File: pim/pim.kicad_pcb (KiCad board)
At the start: 2 copper layers, 76.2 x 33 mm, 3 parts, among them J1 Upper pins, J2 Lower pins

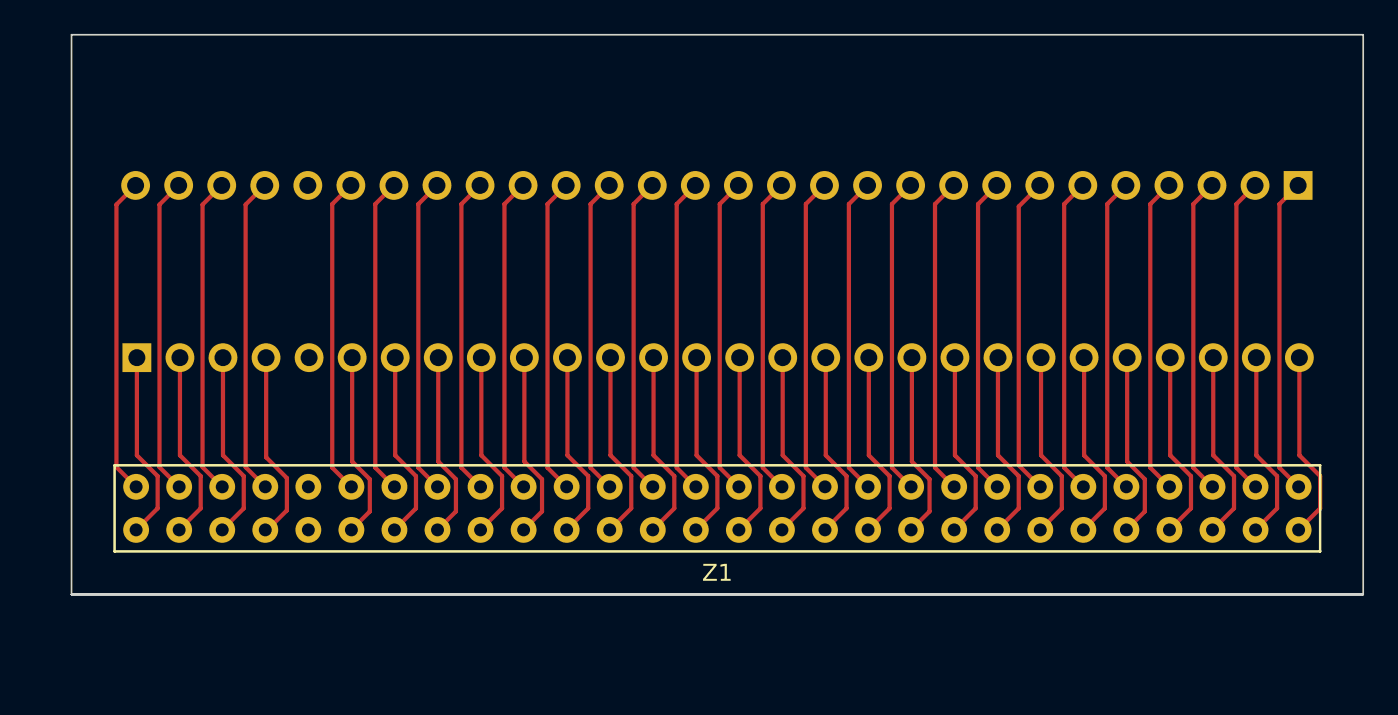
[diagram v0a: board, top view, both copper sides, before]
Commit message: widen connector to match the ones i have
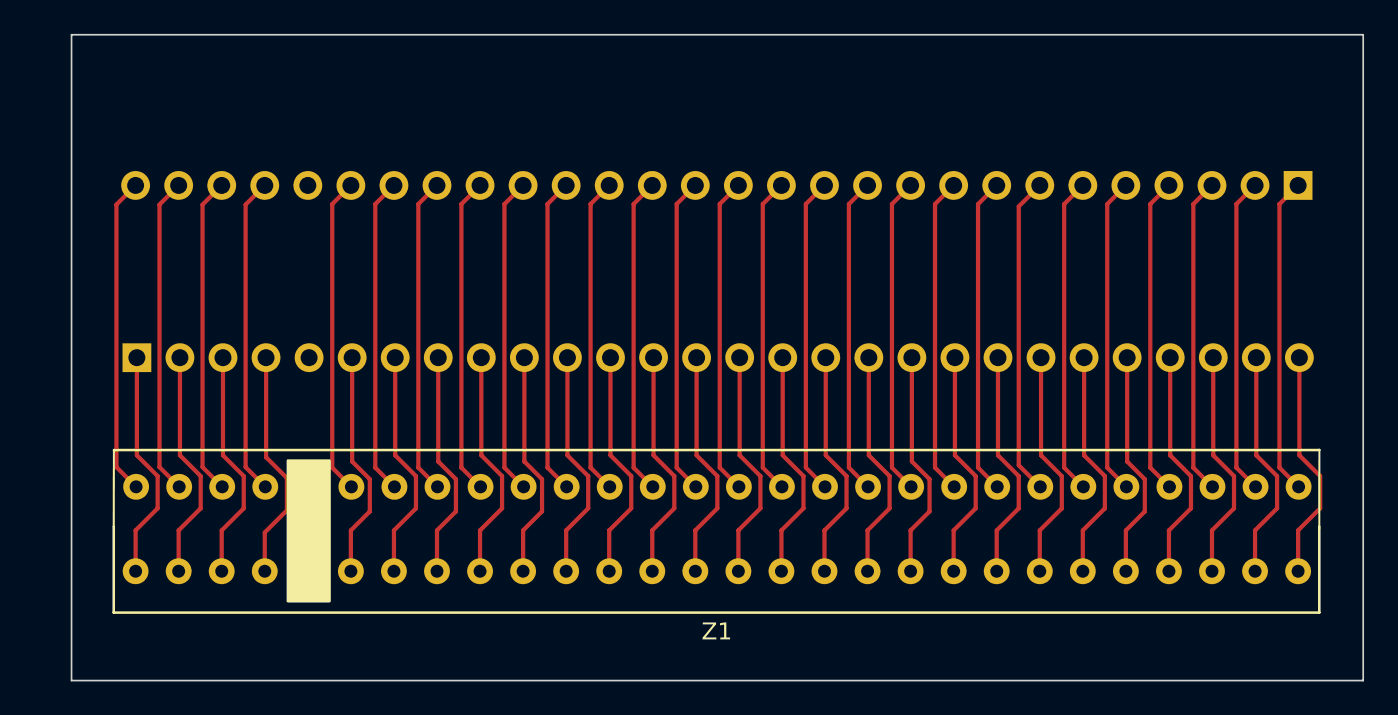
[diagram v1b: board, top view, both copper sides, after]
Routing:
- net V: track 11.2 -> 13.6 mm
- net U: track 11.2 -> 13.6 mm
- net ROMCS: track 11.2 -> 13.6 mm
- net IORQGE: track 11.2 -> 13.6 mm
- net GND3: track 11.2 -> 13.6 mm
- net GND2: track 11.2 -> 13.6 mm
- net BUSACK: track 11.2 -> 13.6 mm
- net A7: track 11.2 -> 13.6 mm
- net A6: track 11.2 -> 13.6 mm
- net A3: track 11.2 -> 13.6 mm
- net A2: track 11.2 -> 13.6 mm
- net A14: track 11.2 -> 13.6 mm
- net A11: track 11.2 -> 13.6 mm
- net A0: track 11.2 -> 13.6 mm
- net +5V: track 11.2 -> 13.6 mm
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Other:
- board size 76.2 x 33 mm -> 76.2 x 38.1 mm

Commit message: ready for a v1.0 fab
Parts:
- added ?: , , F.Cu at (174.1, 112.0)
- added ?: , , F.Cu at (133.5, 108.8)
- added ?: , , F.Cu at (131.0, 108.8)
- added ?: , , F.Cu at (141.1, 112.0)
- added ?: , , F.Cu at (171.6, 108.8)
- added ?: , , F.Cu at (161.4, 108.8)
- added ?: , , F.Cu at (146.2, 112.0)
- added ?: , , F.Cu at (125.8, 112.1)
- added ?: , , F.Cu at (120.7, 112.1)
- added ?: , , F.Cu at (115.6, 112.0)
- added ?: , , F.Cu at (128.4, 112.1)
- added ?: , , F.Cu at (151.3, 108.8)
- added ?: , , F.Cu at (118.2, 108.9)
- added ?: , , F.Cu at (163.9, 108.8)
- added ?: , , F.Cu at (156.3, 112.0)
- added ?: , , F.Cu at (181.8, 108.8)
- added ?: , , F.Cu at (128.5, 108.9)
- added ?: , , F.Cu at (179.2, 112.0)
- added ?: , , F.Cu at (169.0, 112.0)
- added ?: , , F.Cu at (138.5, 112.0)
- added ?: , , F.Cu at (163.9, 112.0)
- added ?: , , F.Cu at (113.1, 108.8)
- added ?: , , F.Cu at (120.7, 108.9)
- added ?: , , F.Cu at (156.4, 108.8)
- added ?: , , F.Cu at (136.0, 108.9)
- added ?: , , F.Cu at (130.9, 112.0)
- added ?: , , F.Cu at (176.7, 108.8)
- added ?: , , F.Cu at (158.9, 108.8)
- added ?: , , F.Cu at (174.1, 108.8)
- added ?: , , F.Cu at (136.0, 112.0)
- added ?: , , F.Cu at (125.9, 108.9)
- added ?: , , F.Cu at (148.8, 108.8)
- added ?: , , F.Cu at (179.2, 108.8)
- added ?: , , F.Cu at (169.1, 108.8)
- added ?: , , F.Cu at (181.8, 112.0)
- added ?: , , F.Cu at (153.8, 108.8)
- added ?: , , F.Cu at (148.7, 112.0)
- added ?: , , F.Cu at (118.2, 112.1)
- added ?: , , F.Cu at (115.7, 108.8)
- added ?: , , F.Cu at (166.4, 108.8)
- added ?: , , F.Cu at (166.4, 112.0)
- added ?: , , F.Cu at (151.3, 112.0)
- added ?: , , F.Cu at (161.4, 112.0)
- added ?: , , F.Cu at (153.8, 112.0)
- added ?: , , F.Cu at (143.7, 108.8)
- added ?: , , F.Cu at (146.2, 108.9)
- added ?: , , F.Cu at (133.4, 112.0)
- added ?: , , F.Cu at (138.6, 108.8)
- added ?: , , F.Cu at (158.9, 112.0)
- added ?: , , F.Cu at (113.1, 112.0)
- added ?: , , F.Cu at (143.6, 112.0)
- added ?: , , F.Cu at (141.1, 108.8)
- added ?: , , F.Cu at (171.6, 112.0)
- added ?: , , F.Cu at (176.6, 112.0)
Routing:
- net A3: track 13.6 -> 17.3 mm
- net U: track 13.6 -> 17.3 mm
- net BUSRQ: track 13.5 -> 17.1 mm
- net A11: track 13.6 -> 17.3 mm
- net Y: track 13.6 -> 17.3 mm
- net A9: track 13.6 -> 17.3 mm
- net A0: track 13.6 -> 17.2 mm
- net RESET: track 13.6 -> 17.2 mm
- net ROMCS: track 13.6 -> 17.2 mm
- net V: track 13.6 -> 17.2 mm
- net A7: track 13.6 -> 17.2 mm
- net IORQGE: track 13.6 -> 17.2 mm
- net A4: track 13.5 -> 17.1 mm
- net CLK: track 13.5 -> 17.1 mm
- net A5: track 13.6 -> 17.2 mm
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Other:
- board size 76.2 x 38.1 mm -> 76.2 x 34.5 mm
- board text added: "+12V"
- board text added: "+12VAC"
- board text added: "+5V"
- board text added: "+9V"
- board text added: "-5V"
- board text added: "A0"
- board text added: "A1"
- board text added: "A10"
- board text added: "A11"
- board text added: "A12"
- board text added: "A13"
- board text added: "A14"
- board text added: "A15"
- board text added: "A2"
- board text added: "A3"
- board text added: "A4"
- board text added: "A5"
- board text added: "A6"
- board text added: "A7"
- board text added: "A8"
- board text added: "A9"
- board text added: "BUSACK"
- board text added: "BUSRQ"
- board text added: "CLK"
- board text added: "D0"
- board text added: "D1"
- board text added: "D2"
- board text added: "D3"
- board text added: "D4"
- board text added: "D5"
- board text added: "D6"
- board text added: "D7"
- board text added: "GND"
- board text added: "HALT"
- board text added: "INT"
- board text added: "IORQ"
- board text added: "IORQGE"
- board text added: "M1"
- board text added: "MREQ"
- board text added: "NC"
- board text added: "NMI"
- board text added: "RD"
- board text added: "RESET"
- board text added: "RFSH"
- board text added: "ROMCS"
- board text added: "U"
- board text added: "V"
- board text added: "VIDEO"
- board text added: "WAIT"
- board text added: "WR"
- board text added: "Y"
- board text added: "github.com/derekfountain/zx-spectrum-plugin-module v1.0"

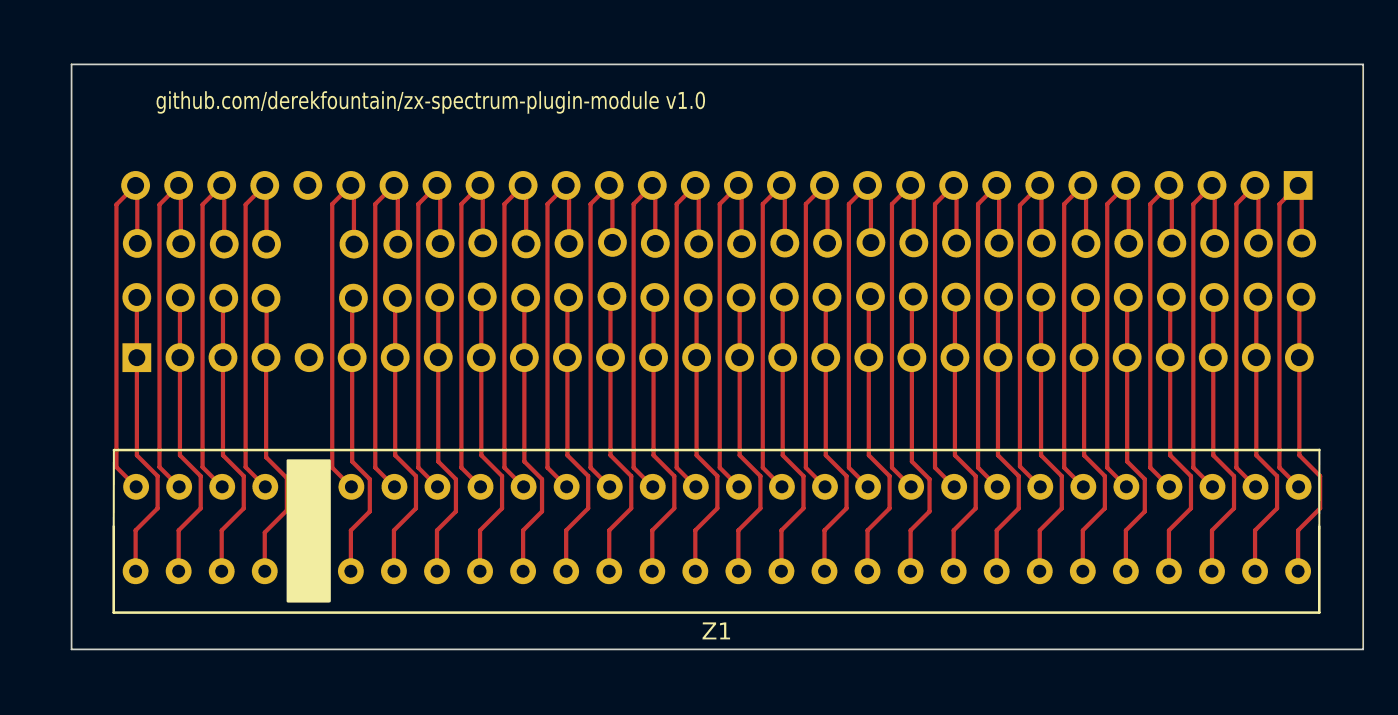
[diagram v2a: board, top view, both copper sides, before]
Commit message: breakout idea separated, i'm not convinced it's useful
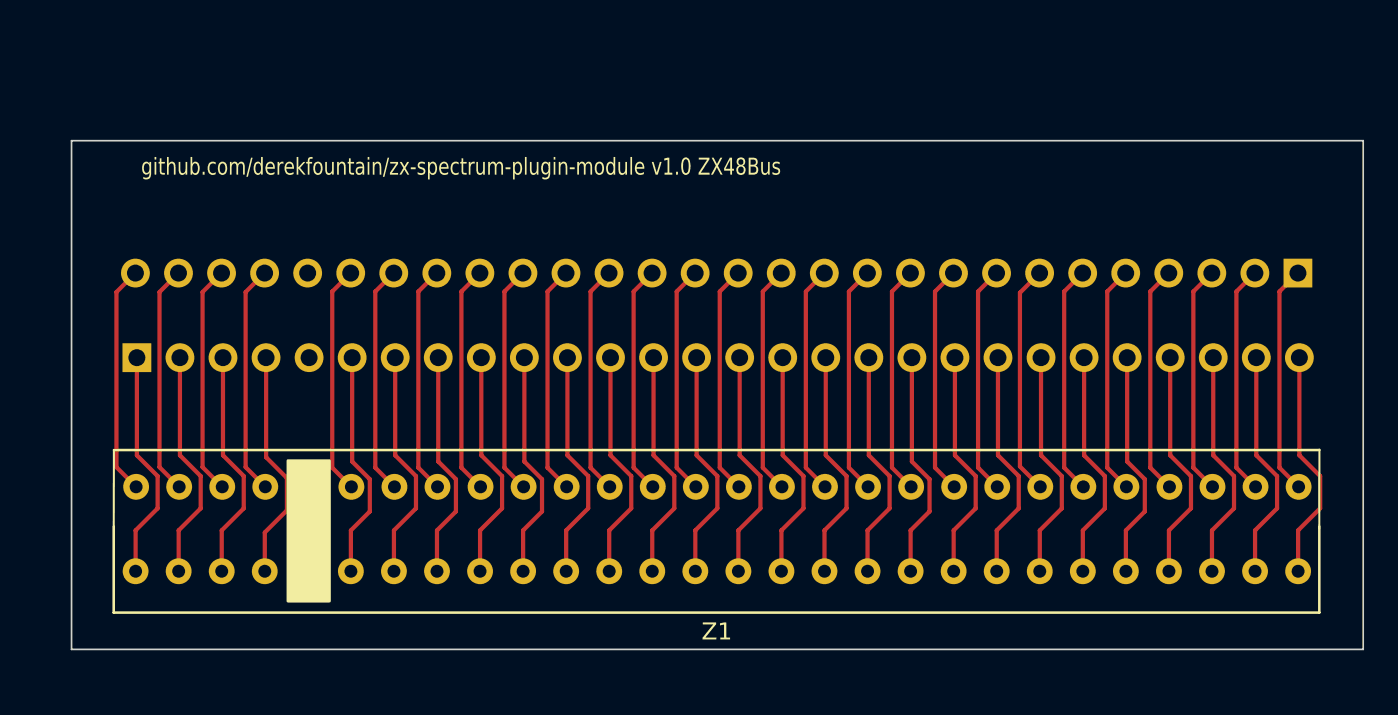
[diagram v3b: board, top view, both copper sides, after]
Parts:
- removed ? (x54): , 
- moved J1 5.17 mm to (181.6, 110.6)
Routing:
- net D1: track 22.3 -> 13.5 mm
- net D0: track 22.2 -> 13.5 mm
- net NMI: track 22.2 -> 13.5 mm
- net D5: track 22.2 -> 13.5 mm
- net D7: track 22.3 -> 13.6 mm
- net HALT: track 22.2 -> 13.5 mm
- net +12VAC: track 22.2 -> 13.5 mm
- net D2: track 22.2 -> 13.5 mm
- net D3: track 22.2 -> 13.5 mm
- net INT: track 22.2 -> 13.5 mm
- net A13: track 22.2 -> 13.6 mm
- net M1: track 22.2 -> 13.5 mm
- net NC2: track 22.2 -> 13.5 mm
- net A8: track 22.2 -> 13.5 mm
- net IORQ: track 22.2 -> 13.5 mm
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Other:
- board size 76.2 x 34.5 mm -> 76.2 x 30 mm
- board text added: "ZX connector pads and holes are small, but if I make them any larger it'll be difficult to get 2 traces between them. Do I care? It's a tight mechanical fit on that ZX connector, which is fine except it makes desoldering the connector difficult. I tried creating a version which uses 2 rows of header sockets instead of that connector, but I can't copy and paste what I have onto the other layer - K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"
- board text added: "github.com/derekfountain/zx-spectrum-plugin-module v1.0 ZX48Bus"
- board text removed: "github.com/derekfountain/zx-spectrum-plugin-module v1.0"
